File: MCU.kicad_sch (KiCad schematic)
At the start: 21 parts, among them J1 USB_B_Micro, J2 Conn_01x04_Pin, SW1 SW_SPDT, U1 STM32F103CBTx, U2 TLV70012_SOT23-5

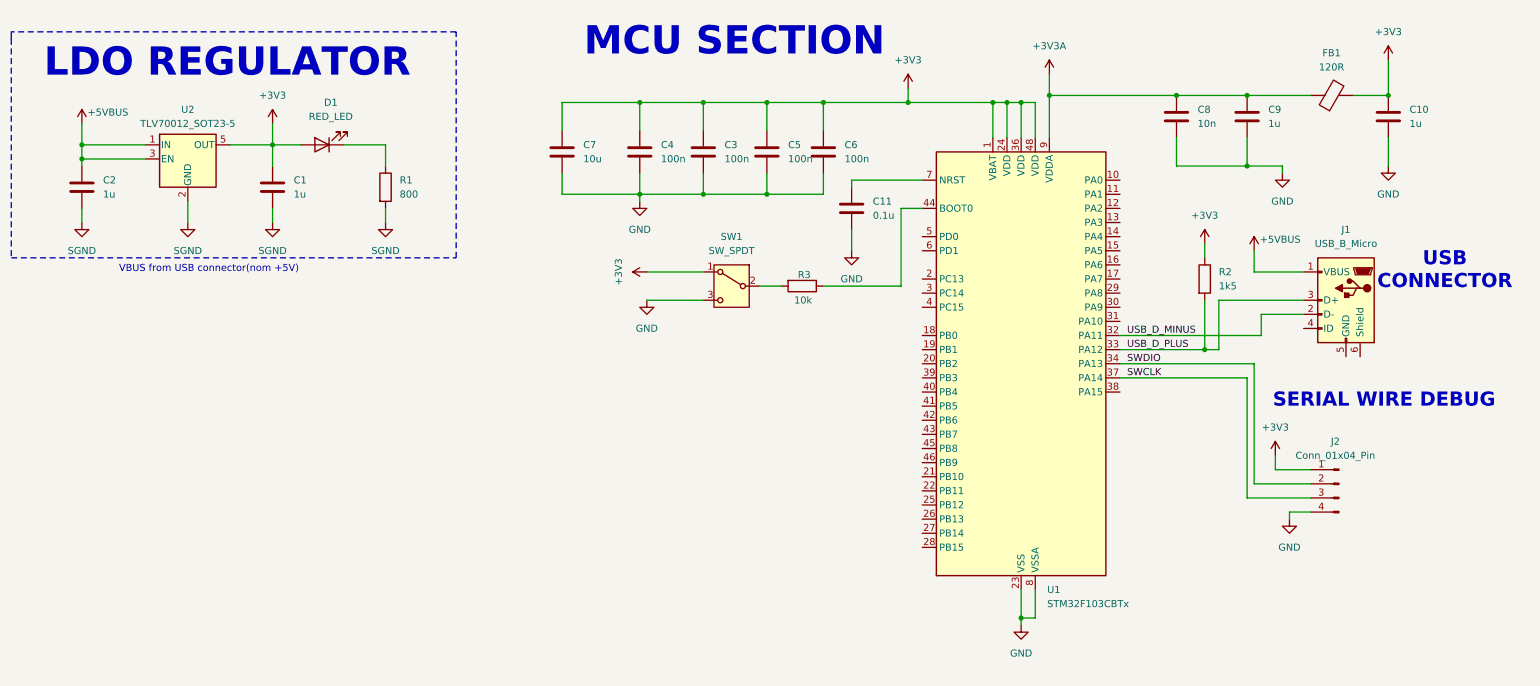
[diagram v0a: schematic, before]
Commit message: MCU Section partially finished
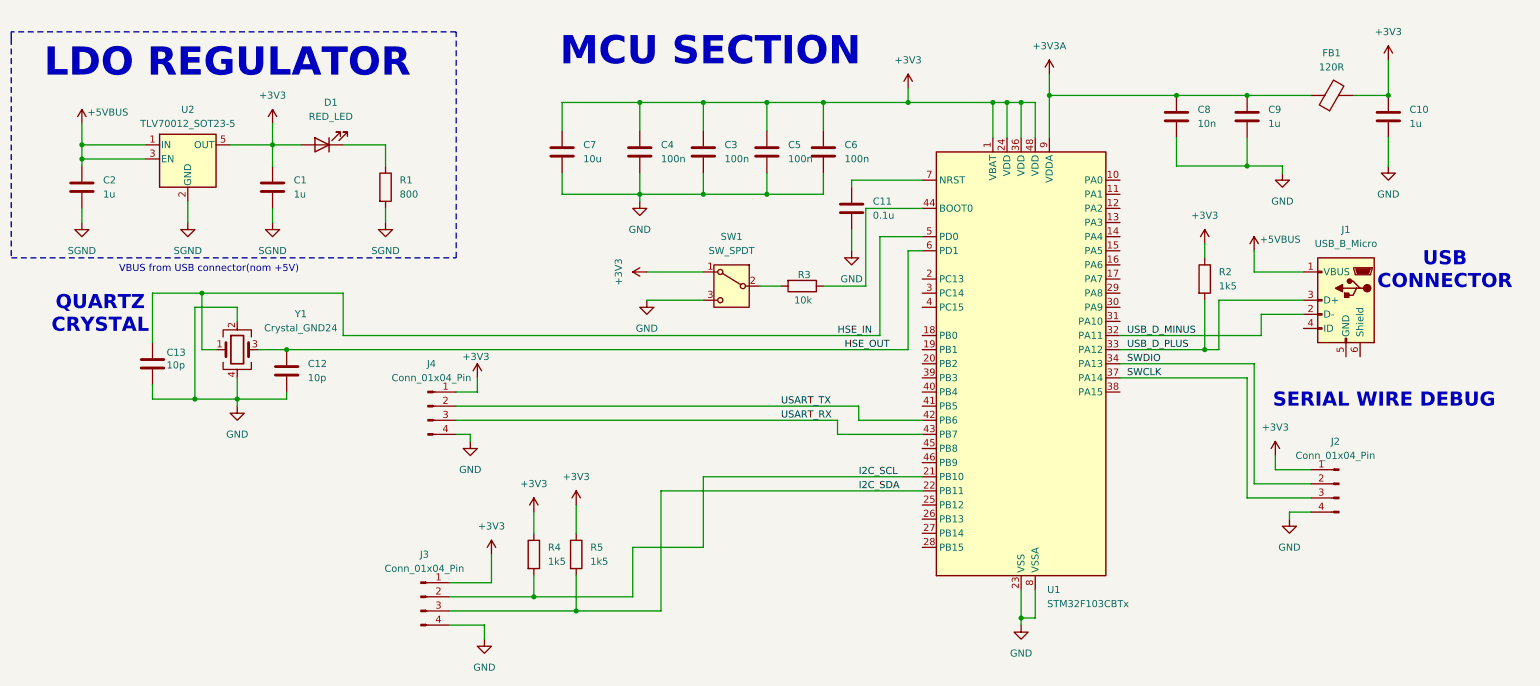
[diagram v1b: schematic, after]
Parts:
- added C12, C13: 10p, symbol Device:C
- added J3, J4: Conn_01x04_Pin, symbol Connector:Conn_01x04_Pin
- added R4, R5: 1k5, symbol Device:R
- added Y1: Crystal_GND24, symbol Device:Crystal_GND24
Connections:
- net +3V3: now also J3.1 (Pin_1), J4.1 (Pin_1), R4.1, R5.1
- net GND: now also C12.2, C13.2, J3.4 (Pin_4), J4.4 (Pin_4), Y1.2, Y1.4
- net I2C_SCL: now reaches U1.21 (PB10)
- net I2C_SCL: now also J3.2 (Pin_2), R4.2
- net I2C_SDA: now reaches U1.22 (PB11)
- net I2C_SDA: now also J3.3 (Pin_3), R5.2
- net USART_TX: now reaches U1.42 (PB6)
- net USART_TX: now also J4.2 (Pin_2)
- net USART_RX: now reaches U1.43 (PB7)
- net USART_RX: now also J4.3 (Pin_3)
- net HSE_IN: now reaches U1.5 (PD0)
- net HSE_IN: now also C13.1, Y1.1
- net HSE_OUT: now reaches U1.6 (PD1)
- net HSE_OUT: now also C12.1, Y1.3
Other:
- note added: "QUARTZ CRYSTAL"

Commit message: Schematic finished pending of layout
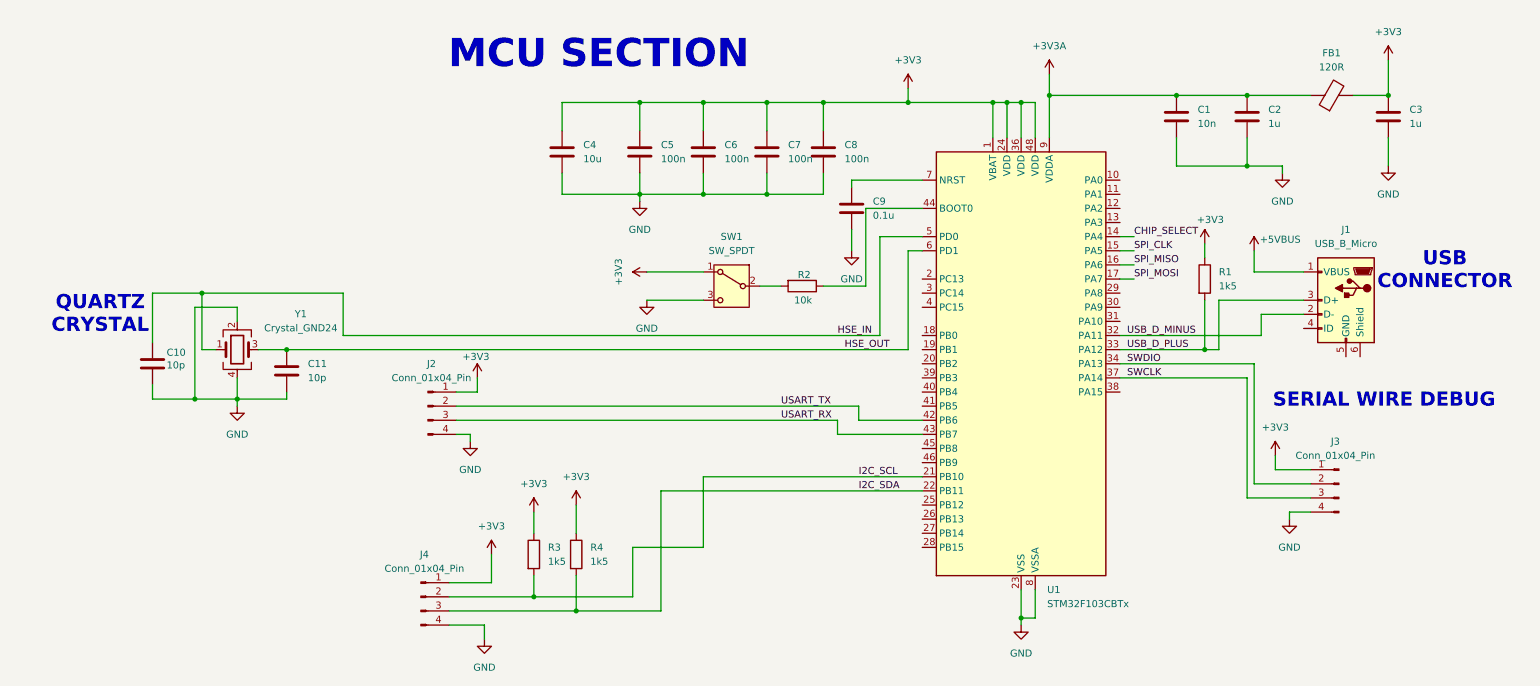
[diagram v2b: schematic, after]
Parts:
- removed C1, C2: 1u, Capacitor_SMD:C_0603_1608Metric, symbol Device:C
- removed D1: RED_LED, symbol Device:LED
- removed R1: 800, Resistor_SMD:R_0603_1608Metric_Pad0.98x0.95mm_HandSolder, symbol Device:R
- removed U2: TLV70012_SOT23-5, Package_TO_SOT_SMD:SOT-23-5, symbol Regulator_Linear:TLV70012_SOT23-5
- renumbered C8 to C1, C13 to C10, C12 to C11, C9 to C2, C10 to C3, C7 to C4, C4 to C5, C3 to C6, C5 to C7, C6 to C8, C11 to C9, J4 to J2, J2 to J3, J3 to J4, R2 to R1, R3 to R2, R4 to R3, R5 to R4
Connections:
- net CHIP_SELECT: now reaches U1.14 (PA4)
- net SPI_CLK: now reaches U1.15 (PA5)
- net SPI_MISO: now reaches U1.16 (PA6)
- net SPI_MOSI: now reaches U1.17 (PA7)
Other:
- note removed: "LDO REGULATOR"
- note removed: "VBUS from USB connector(nom +5V)"
- title: (none) -> MCU Section

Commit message: Commercial components selected
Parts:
- removed Y1: Crystal_GND24, symbol Device:Crystal_GND24
- added Y2: ABLS2-8.000MHZ-D4Y-T, ABLS2-8.000MHZ-D4Y-T:XTAL_ABLS2-8.000MHZ-D4Y-T, symbol ABLS2-8.000MHZ-D4Y-T:ABLS2-8.000MHZ-D4Y-T
- C1: Distributor Link (none) -> https://www.digikey.es/es/products/detail/kemet/C0603C103K5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
- C10, C11: footprint (none) -> Capacitor_SMD:C_0603_1608Metric_Pad1.08x0.95mm_HandSolder; Distributor Link (none) -> https://www.digikey.es/es/products/detail/kemet/C0603C100J5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
- C2, C3: Distributor Link (none) -> https://www.digikey.es/es/products/detail/kemet/C0603C105K4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
- C4: Distributor Link (none) -> https://www.digikey.es/es/products/detail/samsung-electro-m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
- C5, C6, C7, C8: Distributor Link (none) -> https://www.digikey.es/es/products/detail/kemet/C0603C104K5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
- C9: footprint (none) -> Capacitor_SMD:C_0603_1608Metric; Distributor Link (none) -> https://www.digikey.es/es/products/detail/kemet/C0603C104K5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
- FB1: footprint (none) -> Resistor_SMD:R_0805_2012Metric_Pad1.20x1.40mm_HandSolder; Distributor Link (none) -> https://www.digikey.es/es/products/detail/fair-rite-product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
- J1: footprint (none) -> usb_b:CONN_10118194-0001LF_AMP
- J2: footprint (none) -> Connector_PinHeader_2.54mm:PinHeader_1x04_P2.54mm_Vertical; Distributor link (none) -> https://www.digikey.es/es/products/detail/samtec-inc/TS-104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
- J3, J4: footprint (none) -> Connector_PinHeader_2.54mm:PinHeader_1x04_P2.54mm_Vertical; Distributor Link (none) -> https://www.digikey.es/es/products/detail/samtec-inc/TS-104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
- R1, R3, R4: footprint (none) -> Resistor_SMD:R_01005_0402Metric_Pad0.57x0.30mm_HandSolder; Distributor Link (none) -> https://www.digikey.es/es/products/detail/panasonic-electro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
- R2: footprint (none) -> Resistor_SMD:R_0603_1608Metric_Pad0.98x0.95mm_HandSolder; Distributor Link (none) -> https://www.digikey.es/es/products/detail/yageo/RC0603FR-07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
- SW1: footprint (none) -> footprints:CON64_2X32_TU_HTS_SAI_CUSTOM; Distributor Link (none) -> https://www.digikey.es/es/products/detail/samtec-inc/TD-132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
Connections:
- net GND: now also C10.1, C11.1, J1.5 (GND); no longer C10.2, C11.2
- net HSE_IN: now also C11.2, Y2.1; no longer C10.1
- net HSE_OUT: now also C10.2, Y2.2; no longer C11.1
- net +5VBUS renamed USB POWER
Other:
- moved on the sheet: C10, C11

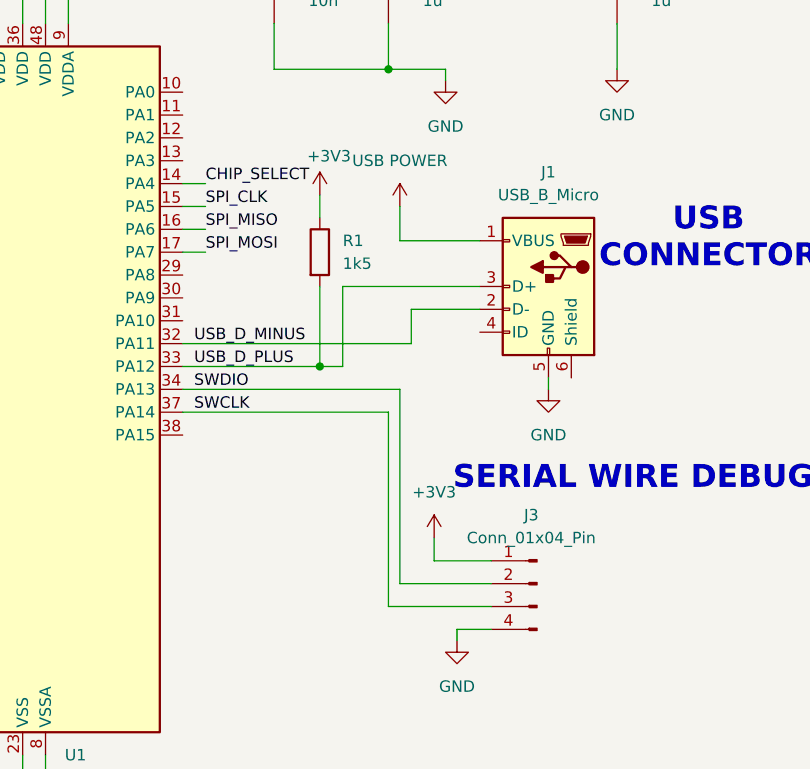
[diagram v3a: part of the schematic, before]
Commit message: over-voltage protection added
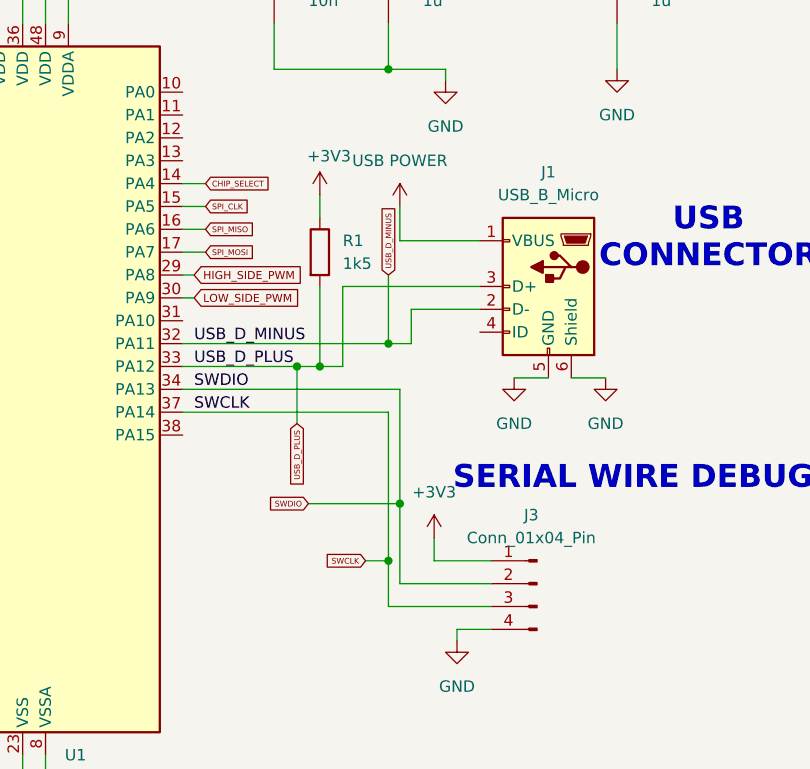
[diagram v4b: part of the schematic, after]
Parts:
- J1: Distributor Link (none) -> https://www.digikey.es/es/products/detail/amphenol-cs-fci/1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
- Y2: footprint ABLS2-8.000MHZ-D4Y-T:XTAL_ABLS2-8.000MHZ-D4Y-T -> Library:XTAL_ABLS2-8.000MHZ-D4Y-T; Distributor Link (none) -> https://www.digikey.es/es/products/detail/abracon-llc/ABLS2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
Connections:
- net GND: now also J1.6 (Shield)
- net HIGH_SIDE_PWM: now reaches U1.29 (PA8)
- net LOW_SIDE_PWM: now reaches U1.30 (PA9)

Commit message: Placement finished routing started
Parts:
- added R28: 10k, Resistor_SMD:R_0402_1005Metric_Pad0.72x0.64mm_HandSolder, symbol Device:R
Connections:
- net GND: now also R28.2
- net ALERT: now reaches U1.26 (PB13)
- net ENABLE: now reaches U1.27 (PB14)
- net LATCH: now reaches U1.28 (PB15)
- net LATCH: now also R28.1
- net +3V3A: no longer names the net of C1.1, C2.1, FB1.1, U1.9 (VDDA)
- no-connect marks 0 -> 19
